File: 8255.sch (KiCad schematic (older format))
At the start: 5 parts, among them U10 8255, U11 8255, U12 8255, U8 PAL16L8, U9 4002

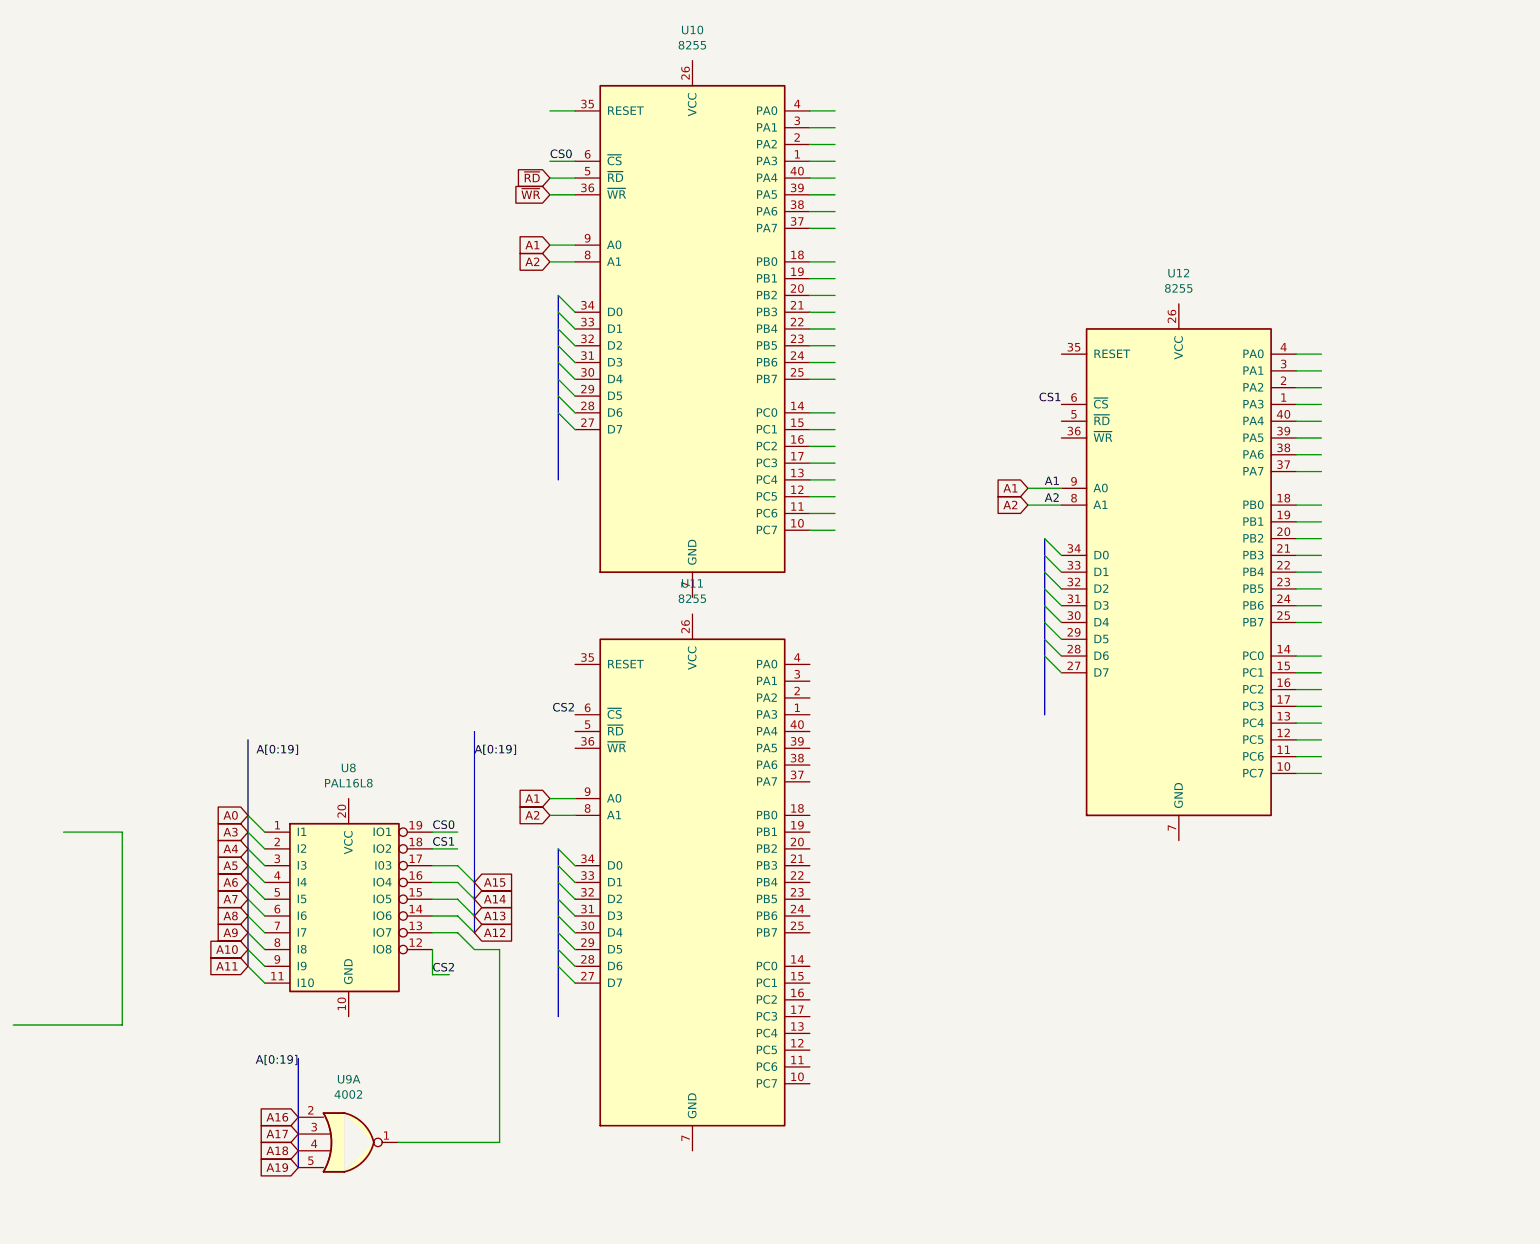
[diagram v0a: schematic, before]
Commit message: 8255 and 8060 schematics
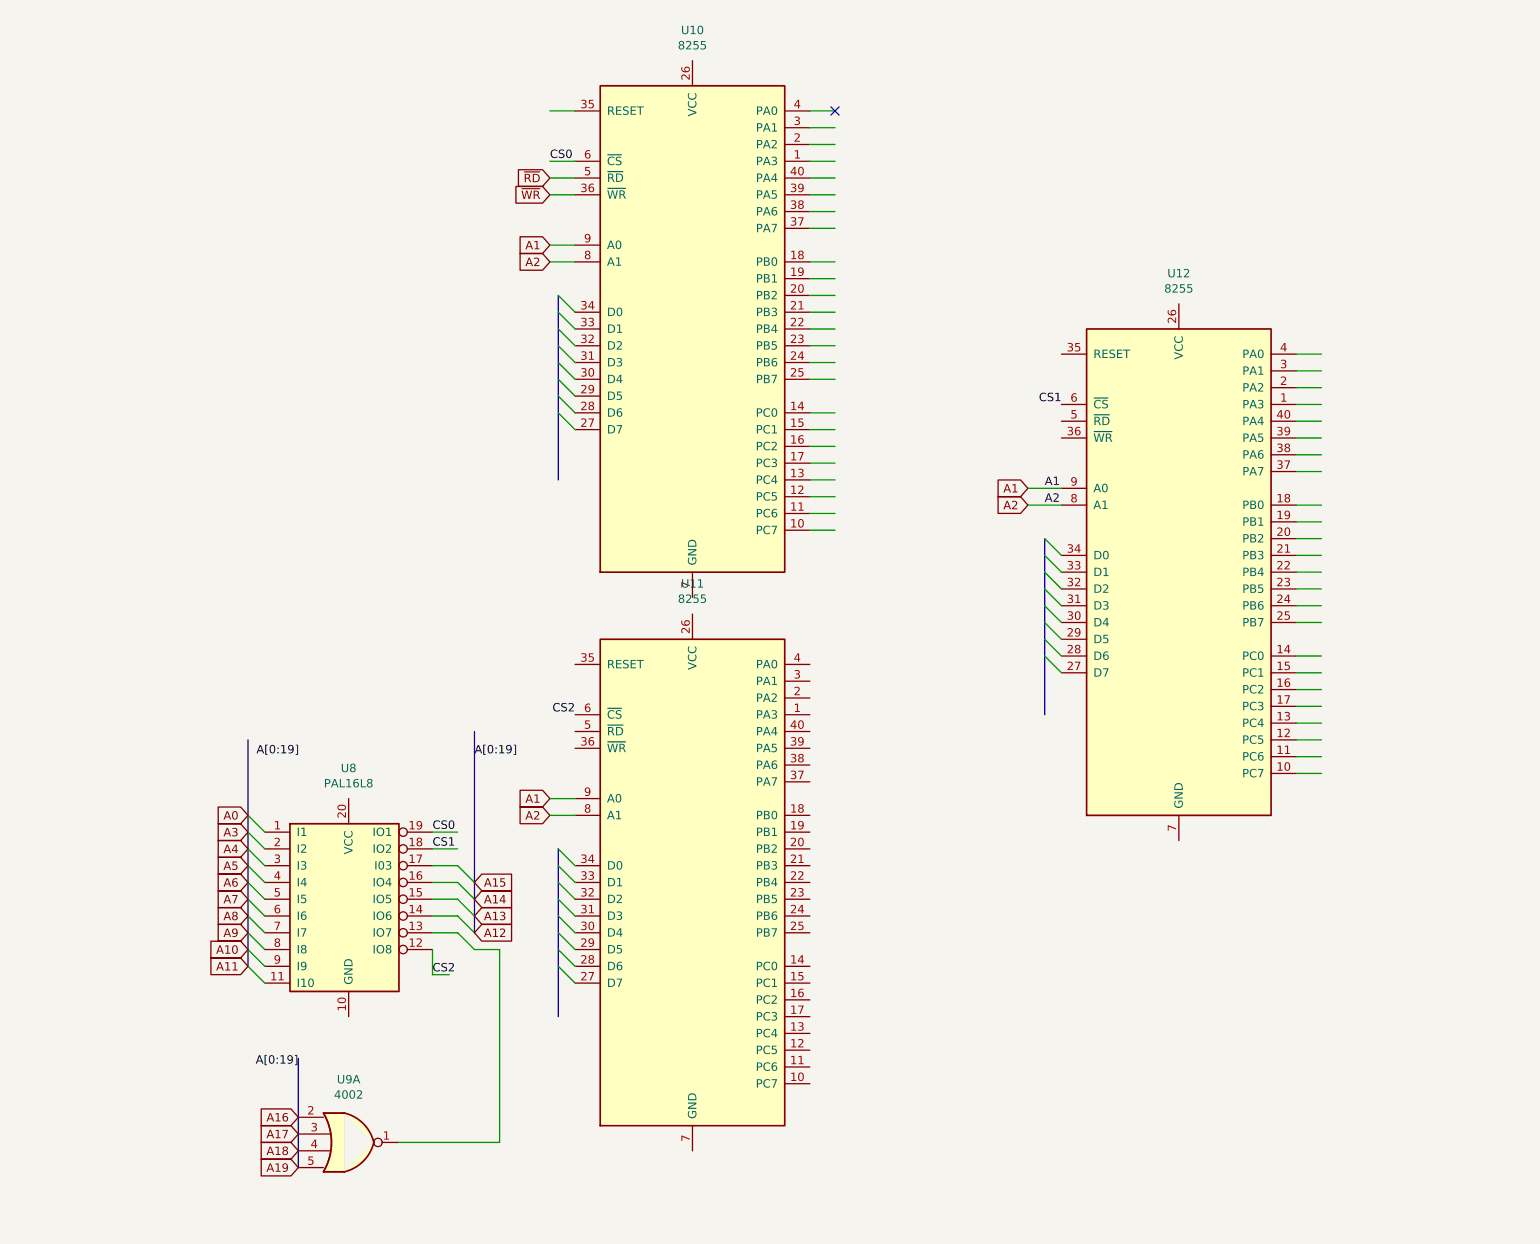
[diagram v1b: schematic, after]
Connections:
- wire segments 73 -> 70
- no-connect marks 0 -> 1
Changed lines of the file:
@@
 Text GLabel 2500 7450 0    50   Input ~ 0
 A19
-Wire Wire Line
-	1100 5450 1450 5450
-Wire Wire Line
-	1450 5450 1450 6600
-Wire Wire Line
-	800  6600 1450 6600
 Text Label 3300 6300 0    50   ~ 0
 CS2
@@
 Text GLabel 4000 1650 0    50   Input ~ 0
 ~WR
+NoConn ~ 5700 1150
 Wire Bus Line
 	3550 4850 3550 6050

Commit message: updated 8086 and 8255 schematic
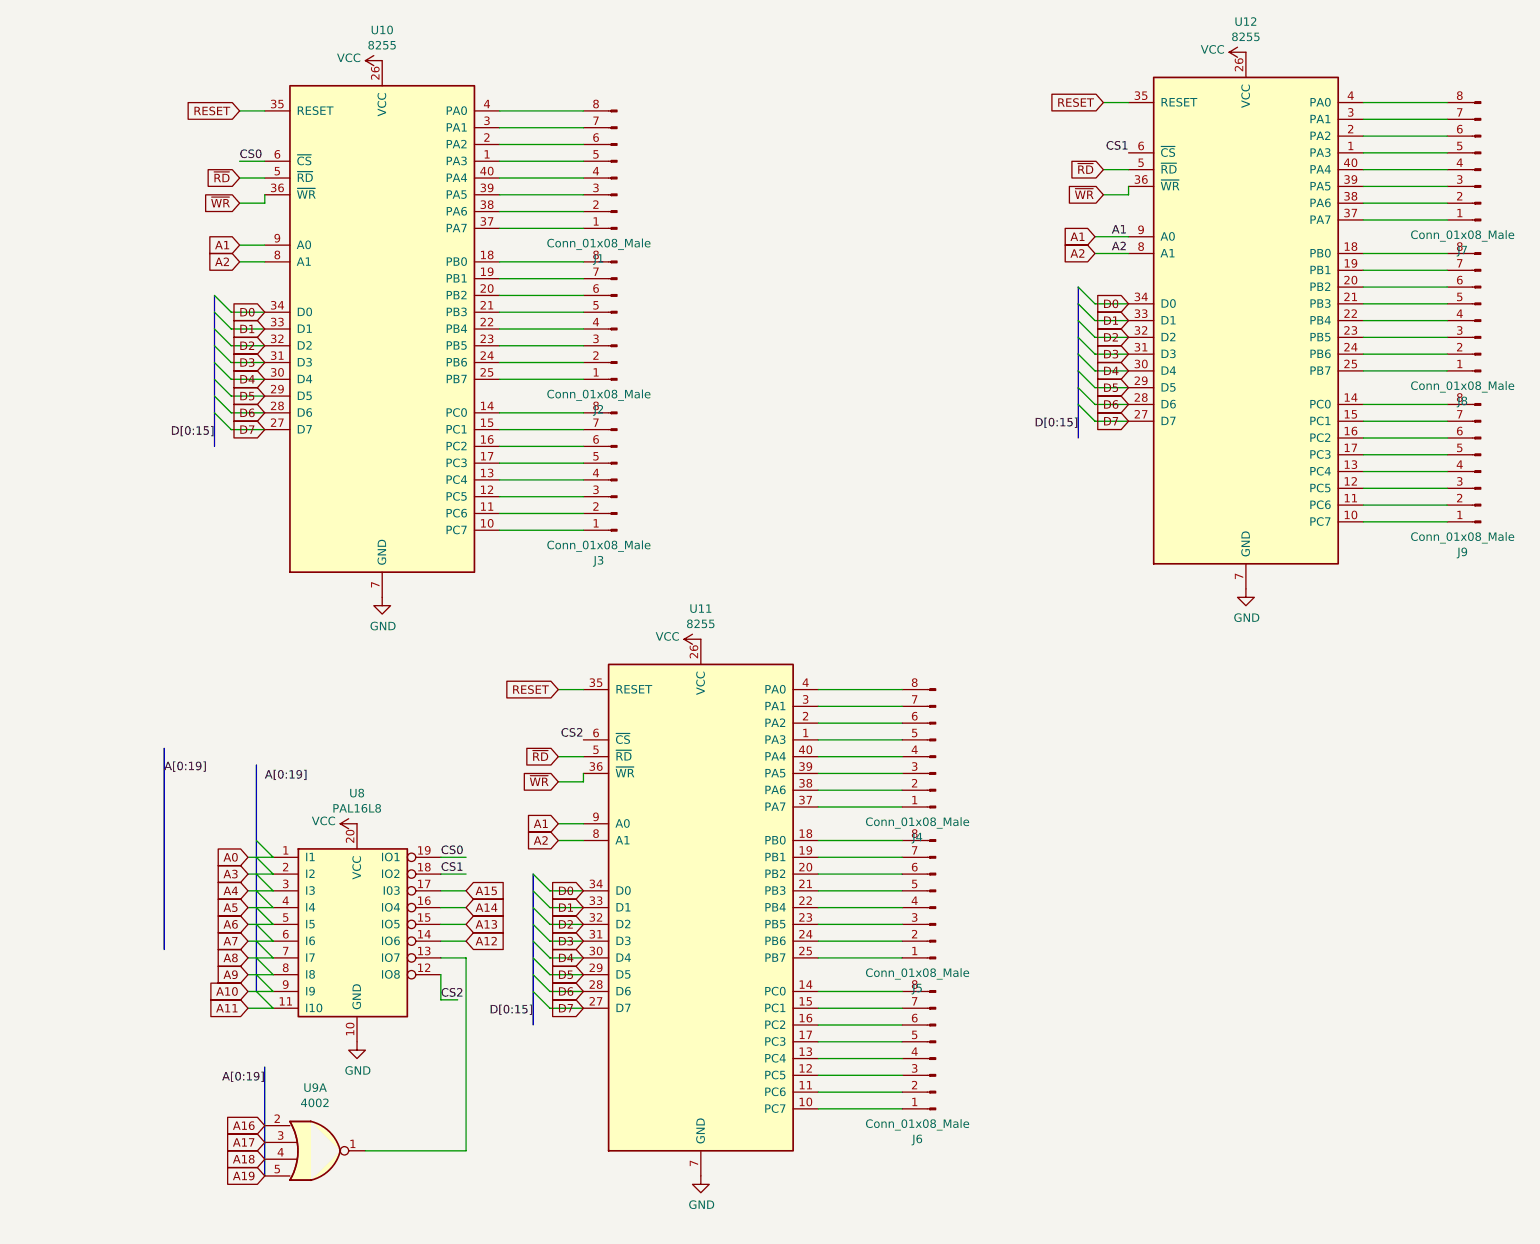
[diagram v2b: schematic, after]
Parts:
- added J1, J2, J3, J4, J5, J6, J7, J8, J9: Conn_01x08_Male, symbol Connector:Conn_01x08_Male
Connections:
- net labels added: D0, D1, D2, D3, D4, D5, D6, D7, D[0:15], GND, RESET, VCC
- wire segments 70 -> 136
- no-connect marks 1 -> 0
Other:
- moved on the sheet: U10, U11, U12, U8, U9A

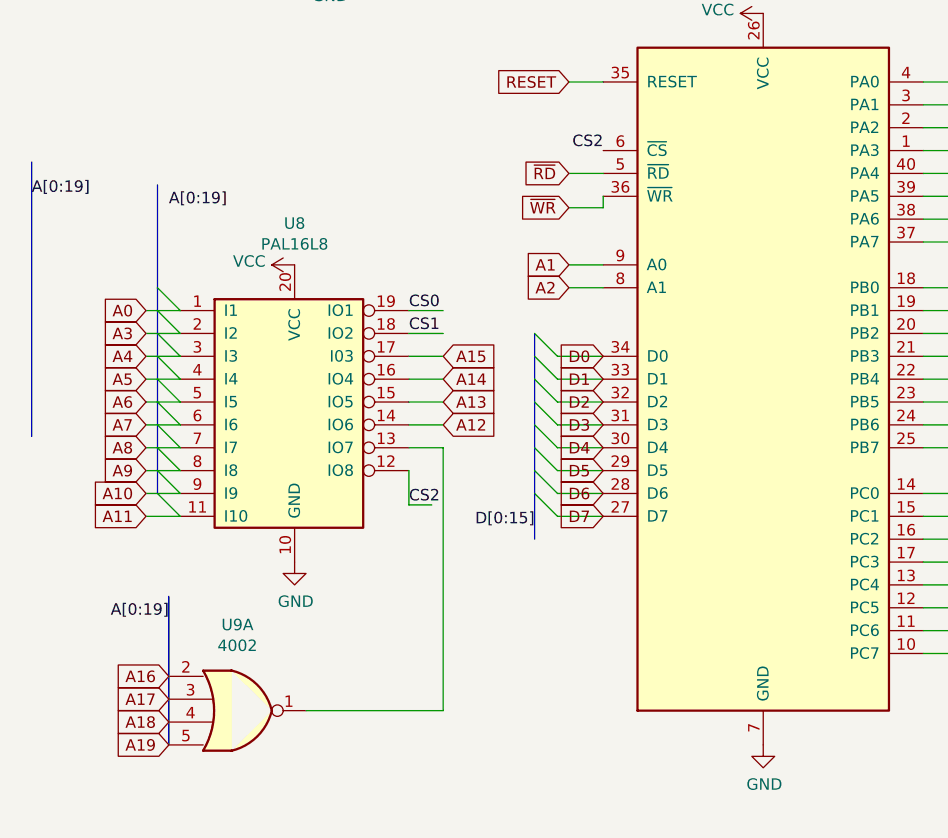
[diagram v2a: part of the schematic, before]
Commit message: Added 16550 UART
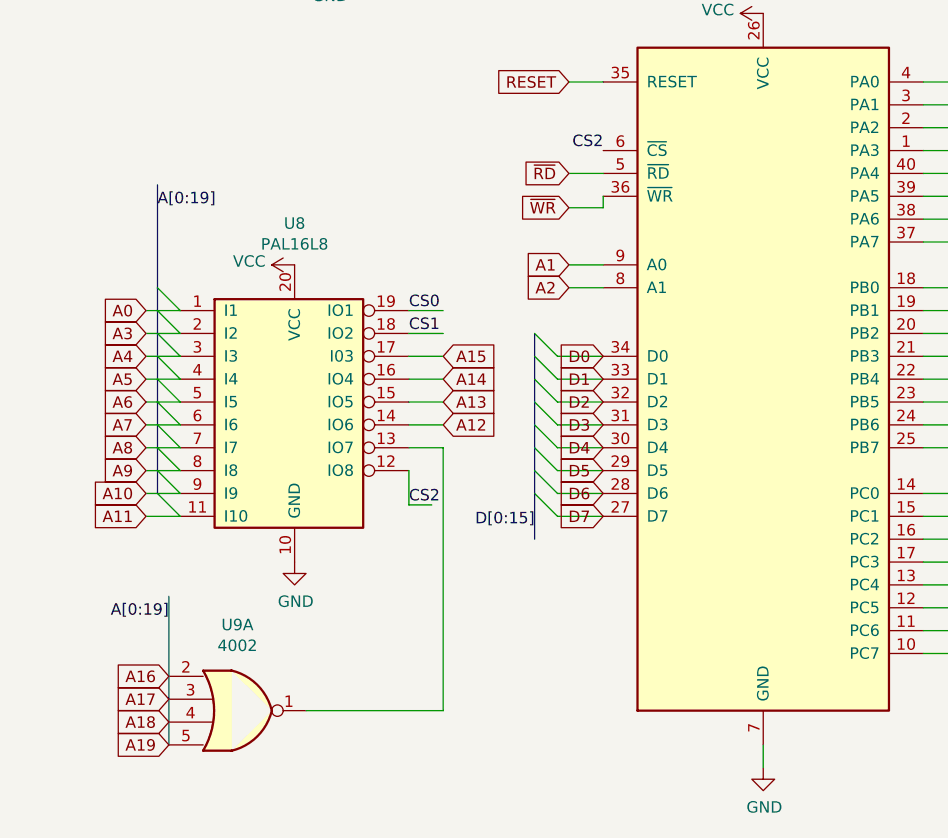
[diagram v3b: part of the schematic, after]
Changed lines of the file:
@@
 $Descr A4 11693 8268
 encoding utf-8
-Sheet 2 2
+Sheet 2 3
 Title ""
 Date ""
@@
 Text Label 3350 5600 0    50   ~ 0
 CS0
-$Comp
-L Logic_Programmable:PAL16L8 U8
-U 1 1 608BEE4C
-P 2850 6100
-F 0 "U8" H 2850 6981 50  0000 C CNN
-F 1 "PAL16L8" H 2850 6890 50  0000 C CNN
-F 2 "" H 2850 6100 50  0001 C CNN
-F 3 "" H 2850 6100 50  0001 C CNN
-	1    2850 6100
-	1    0    0    -1
-$EndComp
 Entry Wire Line
 	2250 5500 2350 5600
@@
 Wire Bus Line
 	2300 6850 2300 7500
-Text Label 2300 5150 0    50   ~ 0
-A[0:19]
-Text Label 1700 5100 0    50   ~ 0
+Text Label 2250 5150 0    50   ~ 0
 A[0:19]
 Text Label 2300 6950 2    50   ~ 0
@@
 L power:GND #PWR0114
 U 1 1 60907C93
-P 4900 7500
-F 0 "#PWR0114" H 4900 7250 50  0001 C CNN
-F 1 "GND" H 4905 7327 50  0000 C CNN
-F 2 "" H 4900 7500 50  0001 C CNN
-F 3 "" H 4900 7500 50  0001 C CNN
-	1    4900 7500
+P 4900 7600
+F 0 "#PWR0114" H 4900 7350 50  0001 C CNN
+F 1 "GND" H 4905 7427 50  0000 C CNN
+F 2 "" H 4900 7600 50  0001 C CNN
+F 3 "" H 4900 7600 50  0001 C CNN
+	1    4900 7600
 	1    0    0    -1
 $EndComp
@@
 Wire Wire Line
 	2350 6500 2200 6500
+Wire Wire Line
+	3500 6200 3500 7350
+Wire Wire Line
+	3350 6200 3500 6200
+Wire Wire Line
+	4900 7500 4900 7600
 Wire Bus Line
-	1700 4950 1700 6150
-Wire Wire Line
-	3500 6200 3500 7350
-Wire Wire Line
-	3350 6200 3500 6200
-Wire Wire Line
-	2200 5600 2350 5600
-Wire Wire Line
-	2200 5700 2350 5700
-Wire Wire Line
-	2200 5800 2350 5800
-Wire Wire Line
-	2200 5900 2350 5900
-Wire Wire Line
-	2200 6000 2350 6000
-Wire Wire Line
-	2200 6100 2350 6100
-Wire Wire Line
-	2200 6200 2350 6200
-Wire Wire Line
-	2200 6300 2350 6300
-Wire Wire Line
-	2200 6400 2350 6400
-Wire Bus Line
-	2250 5050 2250 6400
-Wire Bus Line
-	7150 2200 7150 3100
+	2000 2250 2000 3150
 Wire Bus Line
 	3900 5700 3900 6600
 Wire Bus Line
-	2000 2250 2000 3150
+	7150 2200 7150 3100
+Wire Wire Line
+	2200 6400 2350 6400
+Wire Wire Line
+	2200 6300 2350 6300
+Wire Wire Line
+	2200 6200 2350 6200
+Wire Wire Line
+	2200 6000 2350 6000
+Wire Wire Line
+	2200 5900 2350 5900
+Wire Wire Line
+	2200 5800 2350 5800
+Wire Wire Line
+	2200 5700 2350 5700
+Wire Wire Line
+	2200 5600 2350 5600
+Wire Bus Line
+	2250 5050 2250 6400
+Wire Wire Line
+	2200 6100 2350 6100
+$Comp
+L Logic_Programmable:PAL16L8 U8
+U 1 1 608BEE4C
+P 2850 6100
+F 0 "U8" H 2850 6981 50  0000 C CNN
+F 1 "PAL16L8" H 2850 6890 50  0000 C CNN
+F 2 "" H 2850 6100 50  0001 C CNN
+F 3 "" H 2850 6100 50  0001 C CNN
+	1    2850 6100
+	1    0    0    -1
+$EndComp
 $EndSCHEMATC
